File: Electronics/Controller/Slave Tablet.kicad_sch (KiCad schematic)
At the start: 11 parts, among them J12 SLAVE TABLET, U12 FT232RL, U13 FT232RL

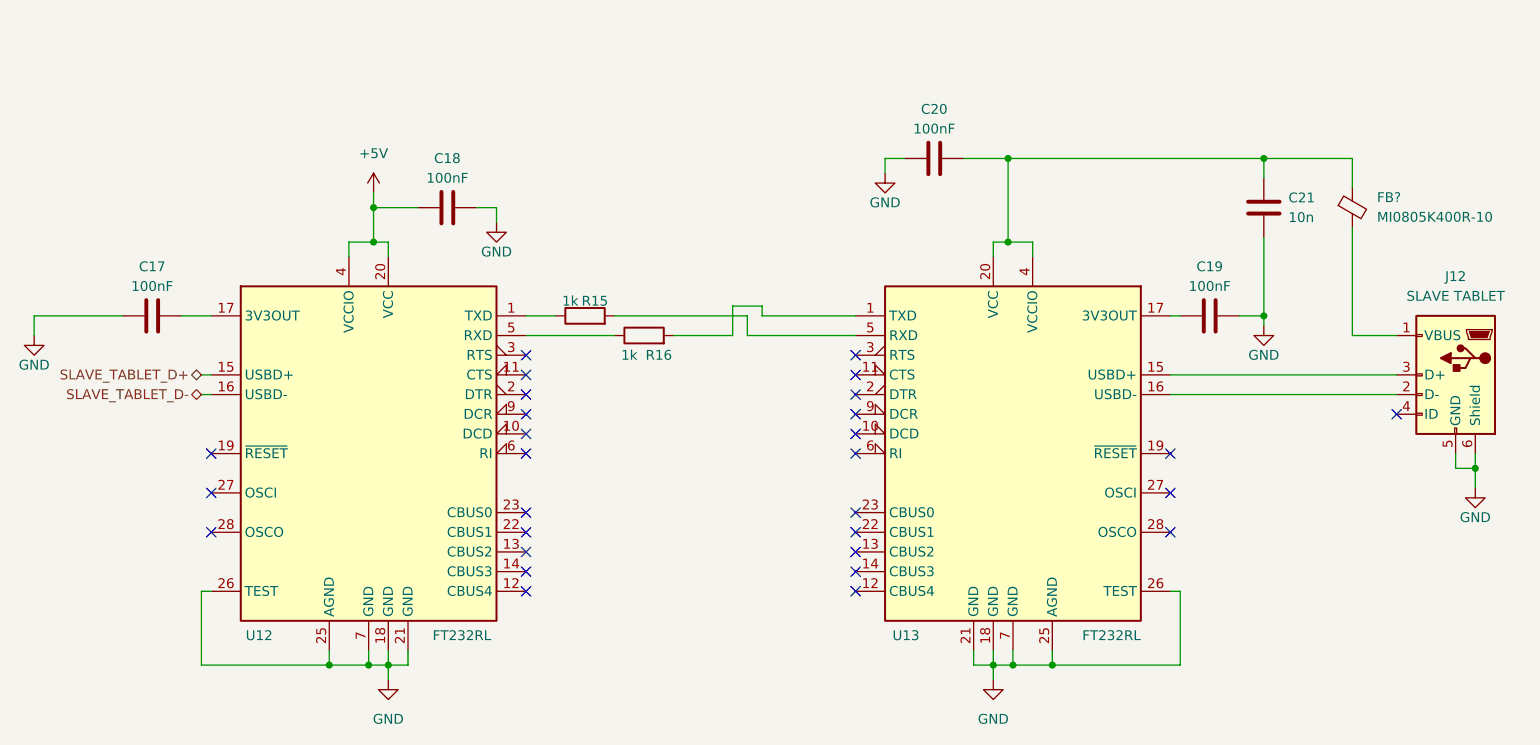
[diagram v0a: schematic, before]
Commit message: Working on schematic. Added datasheets.
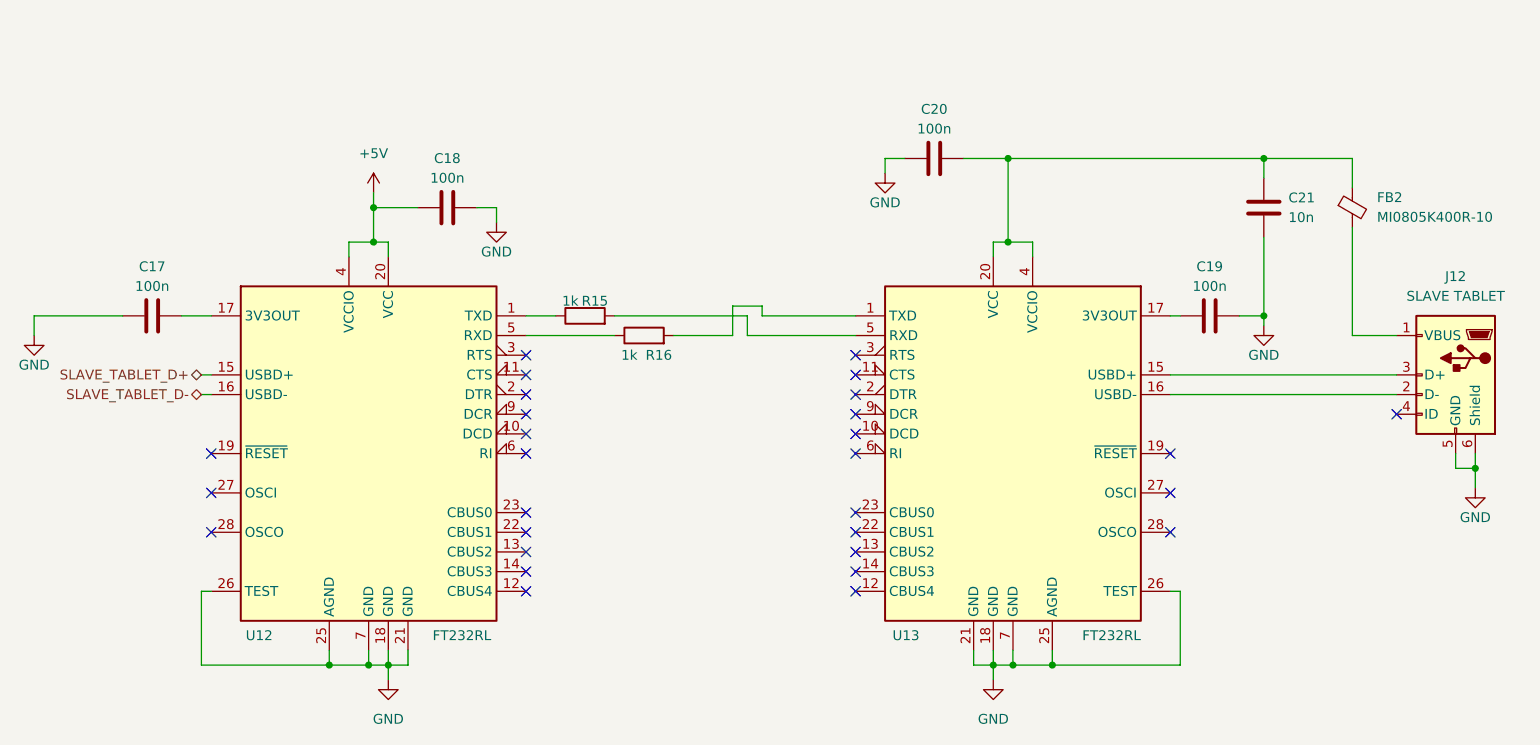
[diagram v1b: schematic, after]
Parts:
- C17, C18, C19, C20: value 100nF -> 100n
- gave numbers to parts that had none: 1
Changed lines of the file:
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@@
   (title_block
     (title "Tandem Leveller Controller")
-    (date "2025-02-13")
+    (date "2025-02-14")
     (rev "V1.0")
     (company "(C) andy@britishideas.com 2025")
@@
       (effects (font (size 1.27 1.27)))
     )
-    (property "Value" "100nF" (at 67.945 78.105 90)
+    (property "Value" "100n" (at 67.945 78.105 90)
       (effects (font (size 1.27 1.27)))
     )
@@
       (effects (font (size 1.27 1.27)))
     )
-    (property "Value" "100nF" (at 204.47 78.105 90)
+    (property "Value" "100n" (at 204.47 78.105 90)
       (effects (font (size 1.27 1.27)))
     )
@@
   (symbol (lib_id "Device:FerriteBead_Small") (at 222.885 67.945 0) (unit 1)
     (in_bom yes) (on_board yes) (dnp no) (fields_autoplaced)
-    (property "Reference" "FB?" (at 226.06 66.6369 0)
+    (property "Reference" "FB2" (at 226.06 66.6369 0)
       (effects (font (size 1.27 1.27)) (justify left))
     )
@@
       (project "Tandem Leveller Controller"
         (path "/56ffd1a6-bbed-43b6-8aa8-f23f49f76448/996de356-8852-43bb-9787-2c246f9a1860"
-          (reference "FB?") (unit 1)
+          (reference "FB2") (unit 1)
         )
       )
@@
       (effects (font (size 1.27 1.27)))
     )
-    (property "Value" "100nF" (at 168.91 57.785 90)
+    (property "Value" "100n" (at 168.91 57.785 90)
       (effects (font (size 1.27 1.27)))
     )
@@
       (effects (font (size 1.27 1.27)))
     )
-    (property "Value" "100nF" (at 106.045 64.135 90)
-      (effects (font (size 1.27 1.27)))
-    )
+    (property "Value" "100n" (at 106.045 64.135 90)
+      (effects (font (size 1.27 1.27)))
+    )

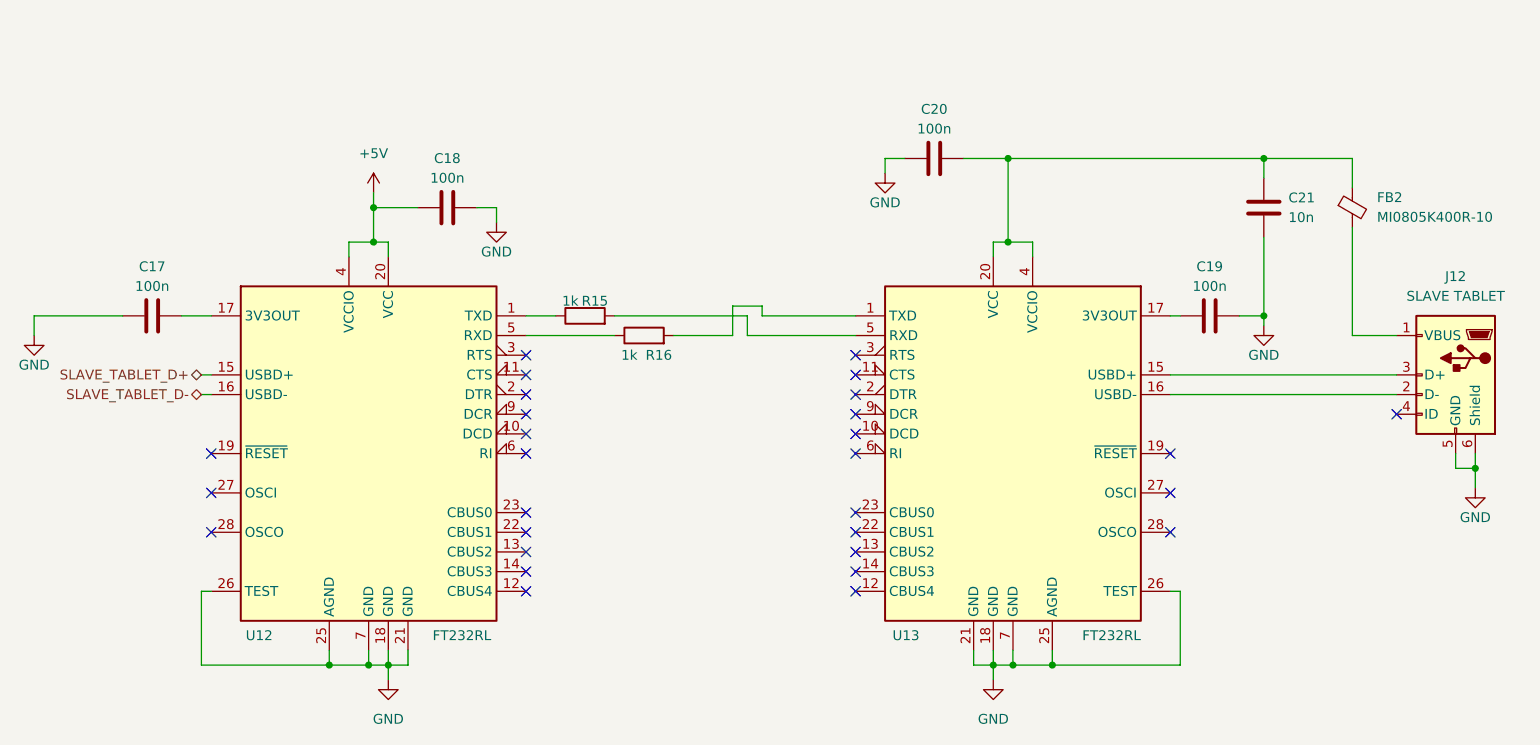
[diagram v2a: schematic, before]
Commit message: Updated schematic. Added footprints for all components.
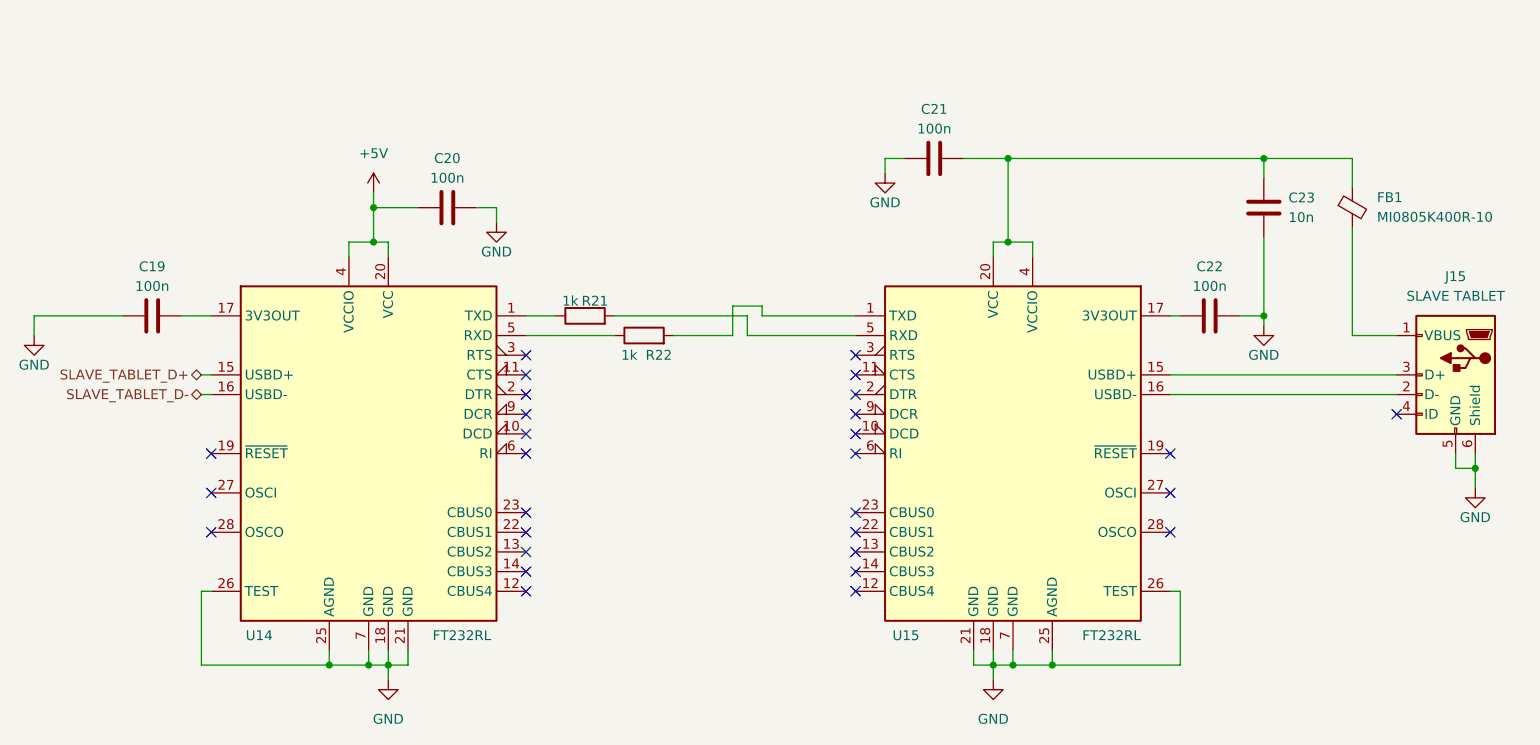
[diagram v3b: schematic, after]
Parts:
- C19: renamed from C17; footprint (none) -> Capacitor_SMD:C_0805_2012Metric
- C20: renamed from C18; footprint (none) -> Capacitor_SMD:C_0805_2012Metric
- C21: renamed from C20; footprint (none) -> Capacitor_SMD:C_0805_2012Metric
- C22: renamed from C19; footprint (none) -> Capacitor_SMD:C_0805_2012Metric
- C23: renamed from C21; footprint (none) -> Capacitor_SMD:C_0805_2012Metric
- J15: renamed from J12; footprint (none) -> Connector_USB:USB_Micro-B_Amphenol_10103594-0001LF_Horizontal; manf# (none) -> 10103594-0001LF
- R21: renamed from R15; footprint (none) -> Resistor_SMD:R_0805_2012Metric
- R22: renamed from R16; footprint (none) -> Resistor_SMD:R_0805_2012Metric
- renumbered FB2 to FB1, U12 to U14, U13 to U15

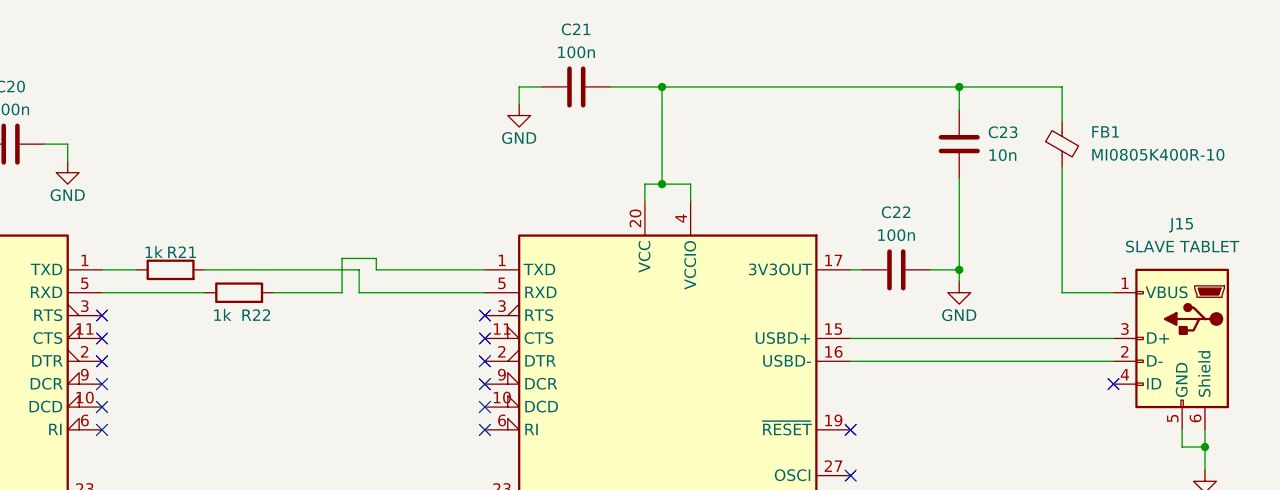
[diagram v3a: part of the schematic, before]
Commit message: Changed switches and lamps. Removed status LEDs. Working on PCB layout.
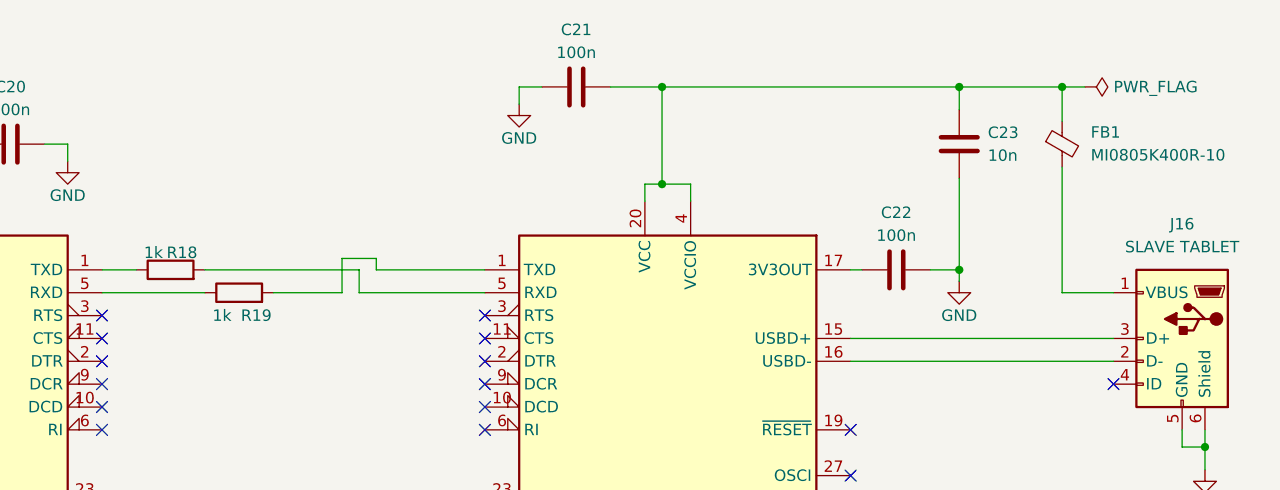
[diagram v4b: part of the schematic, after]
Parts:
- renumbered J15 to J16, R21 to R18, R22 to R19
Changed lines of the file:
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@@
   (title_block
     (title "Tandem Leveller Controller")
-    (date "2025-02-16")
+    (date "2025-02-18")
     (rev "V1.0")
     (company "(C) andy@britishideas.com 2025")
@@
   )
   (junction (at 90.805 127) (diameter 0) (color 0 0 0 0)
+  )
+  (junction (at 222.885 61.595) (diameter 0) (color 0 0 0 0)
   )
   (junction (at 96.52 67.945) (diameter 0) (color 0 0 0 0)
@@
     (stroke (width 0) (type default))
   )
+  (wire (pts (xy 222.885 61.595) (xy 225.425 61.595))
+    (stroke (width 0) (type default))
+  )
   (wire (pts (xy 98.425 72.39) (xy 98.425 74.295))
     (stroke (width 0) (type default))
@@
   (symbol (lib_id "power:+5V") (at 96.52 66.04 0) (unit 1)
     (in_bom yes) (on_board yes) (dnp no) (fields_autoplaced)
-    (property "Reference" "#PWR053" (at 96.52 69.85 0)
+    (property "Reference" "#PWR050" (at 96.52 69.85 0)
       (effects (font (size 1.27 1.27)) hide)
     )
@@
       (project "Tandem Leveller Controller"
         (path "/56ffd1a6-bbed-43b6-8aa8-f23f49f76448/996de356-8852-43bb-9787-2c246f9a1860"
-          (reference "#PWR053") (unit 1)
+          (reference "#PWR050") (unit 1)
         )
       )
@@
   (symbol (lib_id "power:GND") (at 98.425 128.905 0) (unit 1)
     (in_bom yes) (on_board yes) (dnp no) (fields_autoplaced)
-    (property "Reference" "#PWR054" (at 98.425 135.255 0)
+    (property "Reference" "#PWR051" (at 98.425 135.255 0)
       (effects (font (size 1.27 1.27)) hide)
     )
@@
       (project "Tandem Leveller Controller"
         (path "/56ffd1a6-bbed-43b6-8aa8-f23f49f76448/996de356-8852-43bb-9787-2c246f9a1860"
-          (reference "#PWR054") (unit 1)
+          (reference "#PWR051") (unit 1)
         )
       )
@@
   (symbol (lib_id "power:GND") (at 238.76 104.14 0) (mirror y) (unit 1)
     (in_bom yes) (on_board yes) (dnp no)
-    (property "Reference" "#PWR059" (at 238.76 110.49 0)
+    (property "Reference" "#PWR056" (at 238.76 110.49 0)
       (effects (font (size 1.27 1.27)) hide)
     )
@@
       (project "Tandem Leveller Controller"
         (path "/56ffd1a6-bbed-43b6-8aa8-f23f49f76448/996de356-8852-43bb-9787-2c246f9a1860"
-          (reference "#PWR059") (unit 1)
+          (reference "#PWR056") (unit 1)
+        )
+      )
+    )
+  )
+  (symbol (lib_id "power:PWR_FLAG") (at 225.425 61.595 270) (unit 1)
+    (in_bom yes) (on_board yes) (dnp no) (fields_autoplaced)
+    (property "Reference" "#FLG06" (at 227.33 61.595 0)
+      (effects (font (size 1.27 1.27)) hide)
+    )
+    (property "Value" "PWR_FLAG" (at 228.6 61.595 90)
+      (effects (font (size 1.27 1.27)) (justify left))
+    )
+    (property "Footprint" "" (at 225.425 61.595 0)
+      (effects (font (size 1.27 1.27)) hide)
+    )
+    (property "Datasheet" "~" (at 225.425 61.595 0)
+      (effects (font (size 1.27 1.27)) hide)
+    )
+    (pin "1")
+    (instances
+      (project "Tandem Leveller Controller"
+        (path "/56ffd1a6-bbed-43b6-8aa8-f23f49f76448/996de356-8852-43bb-9787-2c246f9a1860"
+          (reference "#FLG06") (unit 1)
         )
       )
@@
   (symbol (lib_id "power:GND") (at 176.53 128.905 0) (mirror y) (unit 1)
     (in_bom yes) (on_board yes) (dnp no) (fields_autoplaced)
-    (property "Reference" "#PWR057" (at 176.53 135.255 0)
+    (property "Reference" "#PWR054" (at 176.53 135.255 0)
       (effects (font (size 1.27 1.27)) hide)
     )
@@
       (project "Tandem Leveller Controller"
         (path "/56ffd1a6-bbed-43b6-8aa8-f23f49f76448/996de356-8852-43bb-9787-2c246f9a1860"
-          (reference "#PWR057") (unit 1)
+          (reference "#PWR054") (unit 1)
         )
       )
@@
   (symbol (lib_id "power:GND") (at 52.705 84.455 0) (unit 1)
     (in_bom yes) (on_board yes) (dnp no)
-    (property "Reference" "#PWR052" (at 52.705 90.805 0)
+    (property "Reference" "#PWR049" (at 52.705 90.805 0)
       (effects (font (size 1.27 1.27)) hide)
     )
@@
       (project "Tandem Leveller Controller"
         (path "/56ffd1a6-bbed-43b6-8aa8-f23f49f76448/996de356-8852-43bb-9787-2c246f9a1860"
-          (reference "#PWR052") (unit 1)
+          (reference "#PWR049") (unit 1)
         )
       )
@@
   (symbol (lib_id "Device:R") (at 123.825 81.915 90) (unit 1)
     (in_bom yes) (on_board yes) (dnp no)
-    (property "Reference" "R21" (at 125.095 80.01 90)
+    (property "Reference" "R18" (at 125.095 80.01 90)
       (effects (font (size 1.27 1.27)))
     )
@@
       (project "Tandem Leveller Controller"
         (path "/56ffd1a6-bbed-43b6-8aa8-f23f49f76448/996de356-8852-43bb-9787-2c246f9a1860"
-          (reference "R21") (unit 1)
+          (reference "R18") (unit 1)
         )
       )
@@
   (symbol (lib_id "Connector:USB_B_Mini") (at 236.22 89.535 0) (mirror y) (unit 1)
     (in_bom yes) (on_board yes) (dnp no)
-    (property "Reference" "J15" (at 236.22 76.835 0)
+    (property "Reference" "J16" (at 236.22 76.835 0)
       (effects (font (size 1.27 1.27)))
     )
@@
       (project "Tandem Leveller Controller"
         (path "/56ffd1a6-bbed-43b6-8aa8-f23f49f76448/996de356-8852-43bb-9787-2c246f9a1860"
-          (reference "J15") (unit 1)
+          (reference "J16") (unit 1)
         )
       )
@@
   (symbol (lib_id "Device:R") (at 131.445 84.455 90) (unit 1)
     (in_bom yes) (on_board yes) (dnp no)
-    (property "Reference" "R22" (at 133.35 86.995 90)
+    (property "Reference" "R19" (at 133.35 86.995 90)
       (effects (font (size 1.27 1.27)))
     )
@@
       (project "Tandem Leveller Controller"
         (path "/56ffd1a6-bbed-43b6-8aa8-f23f49f76448/996de356-8852-43bb-9787-2c246f9a1860"
-          (reference "R22") (unit 1)
+          (reference "R19") (unit 1)
         )
       )
@@
   (symbol (lib_id "power:GND") (at 211.455 83.185 0) (mirror y) (unit 1)
     (in_bom yes) (on_board yes) (dnp no)
-    (property "Reference" "#PWR058" (at 211.455 89.535 0)
+    (property "Reference" "#PWR055" (at 211.455 89.535 0)
       (effects (font (size 1.27 1.27)) hide)
     )
@@
       (project "Tandem Leveller Controller"
         (path "/56ffd1a6-bbed-43b6-8aa8-f23f49f76448/996de356-8852-43bb-9787-2c246f9a1860"
-          (reference "#PWR058") (unit 1)
+          (reference "#PWR055") (unit 1)
         )
       )
@@
   (symbol (lib_id "power:GND") (at 112.395 69.85 0) (unit 1)
     (in_bom yes) (on_board yes) (dnp no)
-    (property "Reference" "#PWR055" (at 112.395 76.2 0)
+    (property "Reference" "#PWR052" (at 112.395 76.2 0)
       (effects (font (size 1.27 1.27)) hide)
     )
@@
       (project "Tandem Leveller Controller"
         (path "/56ffd1a6-bbed-43b6-8aa8-f23f49f76448/996de356-8852-43bb-9787-2c246f9a1860"
-          (reference "#PWR055") (unit 1)
+          (reference "#PWR052") (unit 1)
         )
       )
@@
   (symbol (lib_id "power:GND") (at 162.56 63.5 0) (mirror y) (unit 1)
     (in_bom yes) (on_board yes) (dnp no)
-    (property "Reference" "#PWR056" (at 162.56 69.85 0)
+    (property "Reference" "#PWR053" (at 162.56 69.85 0)
       (effects (font (size 1.27 1.27)) hide)
     )
@@
       (project "Tandem Leveller Controller"
         (path "/56ffd1a6-bbed-43b6-8aa8-f23f49f76448/996de356-8852-43bb-9787-2c246f9a1860"
-          (reference "#PWR056") (unit 1)
-        )
-      )
+          (reference "#PWR053") (unit 1)
+        )
+      )
